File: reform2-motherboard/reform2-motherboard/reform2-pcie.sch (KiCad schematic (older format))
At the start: 31 parts, among them J10 1-2199230-6, J11 48099-5701, U11 679105700

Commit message: reform2 motherboard: add part numbers
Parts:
- C119, C121, C122, C52, C53, C54, C55, C58, C59, C60, C61: Manufacturer TDK -> Yageo; Manufacturer_No CGA3E2X8R1E104K080AE -> CC0603JPX7R9BB104
- C120: Manufacturer Taiyo Yuden -> TDK; Manufacturer_No LMK107BBJ106KALT -> CGA3E2X8R1E104K080AE
- C123, C83: Manufacturer Taiyo Yuden -> Murata; Manufacturer_No LMK107BBJ106KALT -> GRM188R60J476ME15D
- C124, C126: Manufacturer TDK -> Murata; Manufacturer_No CGA3E2X8R1E104K080AE -> GRM188R60J476ME15D
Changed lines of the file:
@@
 F 2 "Capacitor_SMD:C_0603_1608Metric" H 2000 2050 50  0001 C CNN
 F 3 "~" H 2000 2050 50  0001 C CNN
-F 4 "TDK" H 2000 2050 50  0001 C CNN "Manufacturer"
-F 5 "CGA3E2X8R1E104K080AE" H 2000 2050 50  0001 C CNN "Manufacturer_No"
+F 4 "Yageo" H 2000 2050 50  0001 C CNN "Manufacturer"
+F 5 "CC0603JPX7R9BB104" H 2000 2050 50  0001 C CNN "Manufacturer_No"
 	1    2000 2050
 	1    0    0    -1
@@
 F 2 "Capacitor_SMD:C_0603_1608Metric" H 2400 2050 50  0001 C CNN
 F 3 "~" H 2400 2050 50  0001 C CNN
-F 4 "TDK" H 2400 2050 50  0001 C CNN "Manufacturer"
-F 5 "CGA3E2X8R1E104K080AE" H 2400 2050 50  0001 C CNN "Manufacturer_No"
+F 4 "Yageo" H 2400 2050 50  0001 C CNN "Manufacturer"
+F 5 "CC0603JPX7R9BB104" H 2400 2050 50  0001 C CNN "Manufacturer_No"
 	1    2400 2050
 	1    0    0    -1
@@
 F 2 "Capacitor_SMD:C_0603_1608Metric" H 2800 2050 50  0001 C CNN
 F 3 "~" H 2800 2050 50  0001 C CNN
-F 4 "TDK" H 2800 2050 50  0001 C CNN "Manufacturer"
-F 5 "CGA3E2X8R1E104K080AE" H 2800 2050 50  0001 C CNN "Manufacturer_No"
+F 4 "Yageo" H 2800 2050 50  0001 C CNN "Manufacturer"
+F 5 "CC0603JPX7R9BB104" H 2800 2050 50  0001 C CNN "Manufacturer_No"
 	1    2800 2050
 	1    0    0    -1
@@
 F 2 "Capacitor_SMD:C_0603_1608Metric" H 3200 2050 50  0001 C CNN
 F 3 "~" H 3200 2050 50  0001 C CNN
-F 4 "TDK" H 3200 2050 50  0001 C CNN "Manufacturer"
-F 5 "CGA3E2X8R1E104K080AE" H 3200 2050 50  0001 C CNN "Manufacturer_No"
+F 4 "Yageo" H 3200 2050 50  0001 C CNN "Manufacturer"
+F 5 "CC0603JPX7R9BB104" H 3200 2050 50  0001 C CNN "Manufacturer_No"
 	1    3200 2050
 	1    0    0    -1
@@
 F 2 "Capacitor_SMD:C_0603_1608Metric" H 7400 1900 50  0001 C CNN
 F 3 "~" H 7400 1900 50  0001 C CNN
-F 4 "TDK" H 7400 1900 50  0001 C CNN "Manufacturer"
-F 5 "CGA3E2X8R1E104K080AE" H 7400 1900 50  0001 C CNN "Manufacturer_No"
+F 4 "Yageo" H 7400 1900 50  0001 C CNN "Manufacturer"
+F 5 "CC0603JPX7R9BB104" H 7400 1900 50  0001 C CNN "Manufacturer_No"
 	1    7400 1900
 	1    0    0    -1
@@
 F 2 "Capacitor_SMD:C_0603_1608Metric" H 7800 1900 50  0001 C CNN
 F 3 "~" H 7800 1900 50  0001 C CNN
-F 4 "TDK" H 7800 1900 50  0001 C CNN "Manufacturer"
-F 5 "CGA3E2X8R1E104K080AE" H 7800 1900 50  0001 C CNN "Manufacturer_No"
+F 4 "Yageo" H 7800 1900 50  0001 C CNN "Manufacturer"
+F 5 "CC0603JPX7R9BB104" H 7800 1900 50  0001 C CNN "Manufacturer_No"
 	1    7800 1900
 	1    0    0    -1
@@
 F 2 "Capacitor_SMD:C_0603_1608Metric" H 8200 1900 50  0001 C CNN
 F 3 "~" H 8200 1900 50  0001 C CNN
-F 4 "TDK" H 8200 1900 50  0001 C CNN "Manufacturer"
-F 5 "CGA3E2X8R1E104K080AE" H 8200 1900 50  0001 C CNN "Manufacturer_No"
+F 4 "Yageo" H 8200 1900 50  0001 C CNN "Manufacturer"
+F 5 "CC0603JPX7R9BB104" H 8200 1900 50  0001 C CNN "Manufacturer_No"
 	1    8200 1900
 	1    0    0    -1
@@
 F 2 "Capacitor_SMD:C_0603_1608Metric" H 8600 1900 50  0001 C CNN
 F 3 "~" H 8600 1900 50  0001 C CNN
-F 4 "TDK" H 8600 1900 50  0001 C CNN "Manufacturer"
-F 5 "CGA3E2X8R1E104K080AE" H 8600 1900 50  0001 C CNN "Manufacturer_No"
+F 4 "Yageo" H 8600 1900 50  0001 C CNN "Manufacturer"
+F 5 "CC0603JPX7R9BB104" H 8600 1900 50  0001 C CNN "Manufacturer_No"
 	1    8600 1900
 	1    0    0    -1
@@
 F 2 "Capacitor_SMD:C_0603_1608Metric" H 7050 4650 50  0001 C CNN
 F 3 "~" H 7050 4650 50  0001 C CNN
-F 4 "TDK" H 7050 4650 50  0001 C CNN "Manufacturer"
-F 5 "CGA3E2X8R1E104K080AE" H 7050 4650 50  0001 C CNN "Manufacturer_No"
+F 4 "Yageo" H 7050 4650 50  0001 C CNN "Manufacturer"
+F 5 "CC0603JPX7R9BB104" H 7050 4650 50  0001 C CNN "Manufacturer_No"
 	1    7050 4650
 	0    1    1    0
@@
 F 2 "Capacitor_SMD:C_0603_1608Metric" H 6750 4750 50  0001 C CNN
 F 3 "~" H 6750 4750 50  0001 C CNN
-F 4 "TDK" H 6750 4750 50  0001 C CNN "Manufacturer"
-F 5 "CGA3E2X8R1E104K080AE" H 6750 4750 50  0001 C CNN "Manufacturer_No"
+F 4 "Yageo" H 6750 4750 50  0001 C CNN "Manufacturer"
+F 5 "CC0603JPX7R9BB104" H 6750 4750 50  0001 C CNN "Manufacturer_No"
 	1    6750 4750
 	0    1    1    0
@@
 F 2 "Capacitor_SMD:C_0603_1608Metric" H 5200 2400 50  0001 C CNN
 F 3 "~" H 5200 2400 50  0001 C CNN
-F 4 "Taiyo Yuden" H 5200 2400 50  0001 C CNN "Manufacturer"
-F 5 "LMK107BBJ106KALT" H 5200 2400 50  0001 C CNN "Manufacturer_No"
+F 4 "TDK" H 5200 2400 50  0001 C CNN "Manufacturer"
+F 5 "CGA3E2X8R1E104K080AE" H 5200 2400 50  0001 C CNN "Manufacturer_No"
 	1    5200 2400
 	1    0    0    -1
@@
 F 2 "Capacitor_SMD:C_0603_1608Metric" H 4800 2400 50  0001 C CNN
 F 3 "~" H 4800 2400 50  0001 C CNN
-F 4 "TDK" H 4800 2400 50  0001 C CNN "Manufacturer"
-F 5 "CGA3E2X8R1E104K080AE" H 4800 2400 50  0001 C CNN "Manufacturer_No"
+F 4 "Yageo" H 4800 2400 50  0001 C CNN "Manufacturer"
+F 5 "CC0603JPX7R9BB104" H 4800 2400 50  0001 C CNN "Manufacturer_No"
 	1    4800 2400
 	1    0    0    -1
@@
 F 2 "Capacitor_SMD:C_0603_1608Metric" H 3600 2050 50  0001 C CNN
 F 3 "~" H 3600 2050 50  0001 C CNN
-F 4 "Taiyo Yuden" H 3600 2050 50  0001 C CNN "Manufacturer"
-F 5 "LMK107BBJ106KALT" H 3600 2050 50  0001 C CNN "Manufacturer_No"
+F 4 "Murata" H 3600 2050 50  0001 C CNN "Manufacturer"
+F 5 "GRM188R60J476ME15D" H 3600 2050 50  0001 C CNN "Manufacturer_No"
 	1    3600 2050
 	1    0    0    -1
@@
 F 2 "Capacitor_SMD:C_0603_1608Metric" H 4000 2050 50  0001 C CNN
 F 3 "~" H 4000 2050 50  0001 C CNN
-F 4 "Taiyo Yuden" H 4000 2050 50  0001 C CNN "Manufacturer"
-F 5 "LMK107BBJ106KALT" H 4000 2050 50  0001 C CNN "Manufacturer_No"
+F 4 "Murata" H 4000 2050 50  0001 C CNN "Manufacturer"
+F 5 "GRM188R60J476ME15D" H 4000 2050 50  0001 C CNN "Manufacturer_No"
 	1    4000 2050
 	1    0    0    -1
@@
 F 2 "Capacitor_SMD:C_0603_1608Metric" H 9000 1900 50  0001 C CNN
 F 3 "~" H 9000 1900 50  0001 C CNN
-F 4 "TDK" H 9000 1900 50  0001 C CNN "Manufacturer"
-F 5 "CGA3E2X8R1E104K080AE" H 9000 1900 50  0001 C CNN "Manufacturer_No"
+F 4 "Murata" H 9000 1900 50  0001 C CNN "Manufacturer"
+F 5 "GRM188R60J476ME15D" H 9000 1900 50  0001 C CNN "Manufacturer_No"
 	1    9000 1900
 	1    0    0    -1
@@
 F 2 "Capacitor_SMD:C_0603_1608Metric" H 9400 1900 50  0001 C CNN
 F 3 "~" H 9400 1900 50  0001 C CNN
-F 4 "TDK" H 9400 1900 50  0001 C CNN "Manufacturer"
-F 5 "CGA3E2X8R1E104K080AE" H 9400 1900 50  0001 C CNN "Manufacturer_No"
+F 4 "Murata" H 9400 1900 50  0001 C CNN "Manufacturer"
+F 5 "GRM188R60J476ME15D" H 9400 1900 50  0001 C CNN "Manufacturer_No"
 	1    9400 1900
 	1    0    0    -1

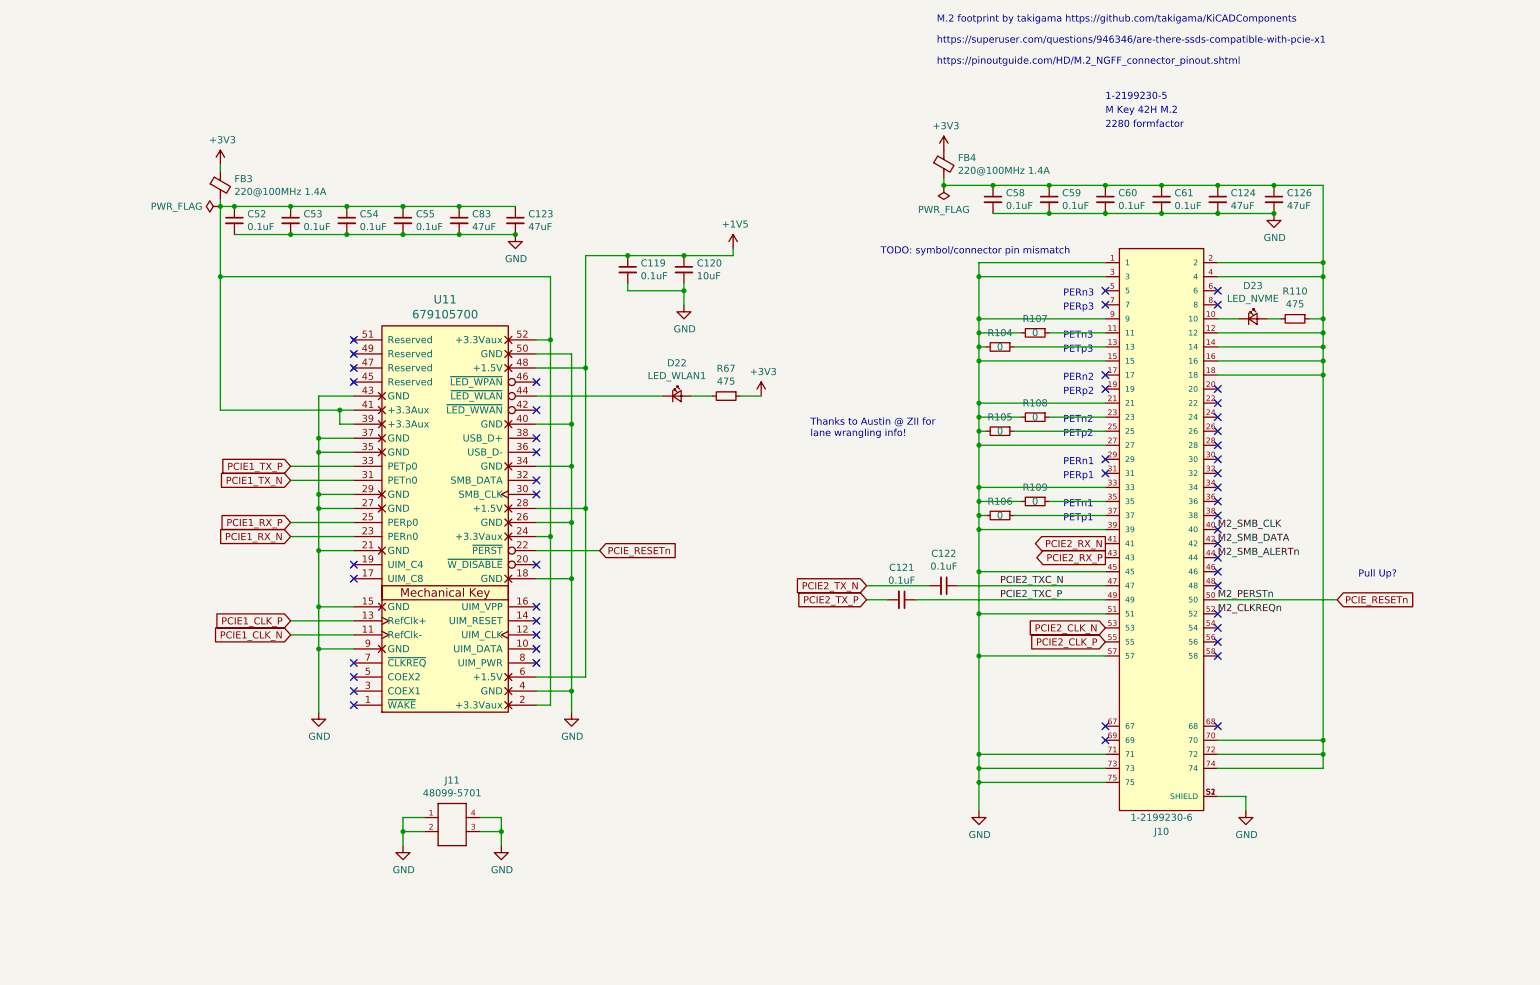
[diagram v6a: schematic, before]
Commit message: Reform 2 Rev 2 WIP: fixed various Rev 1 bugs; consolidate battery connector; consolidate 5v powers; make power rails switchable by LPC; exchange TUSB QFN for TQFP; remove eDP FPC; fixes holes; add SD level shifter; add PCIe clock generator; reduce JTAG footprint
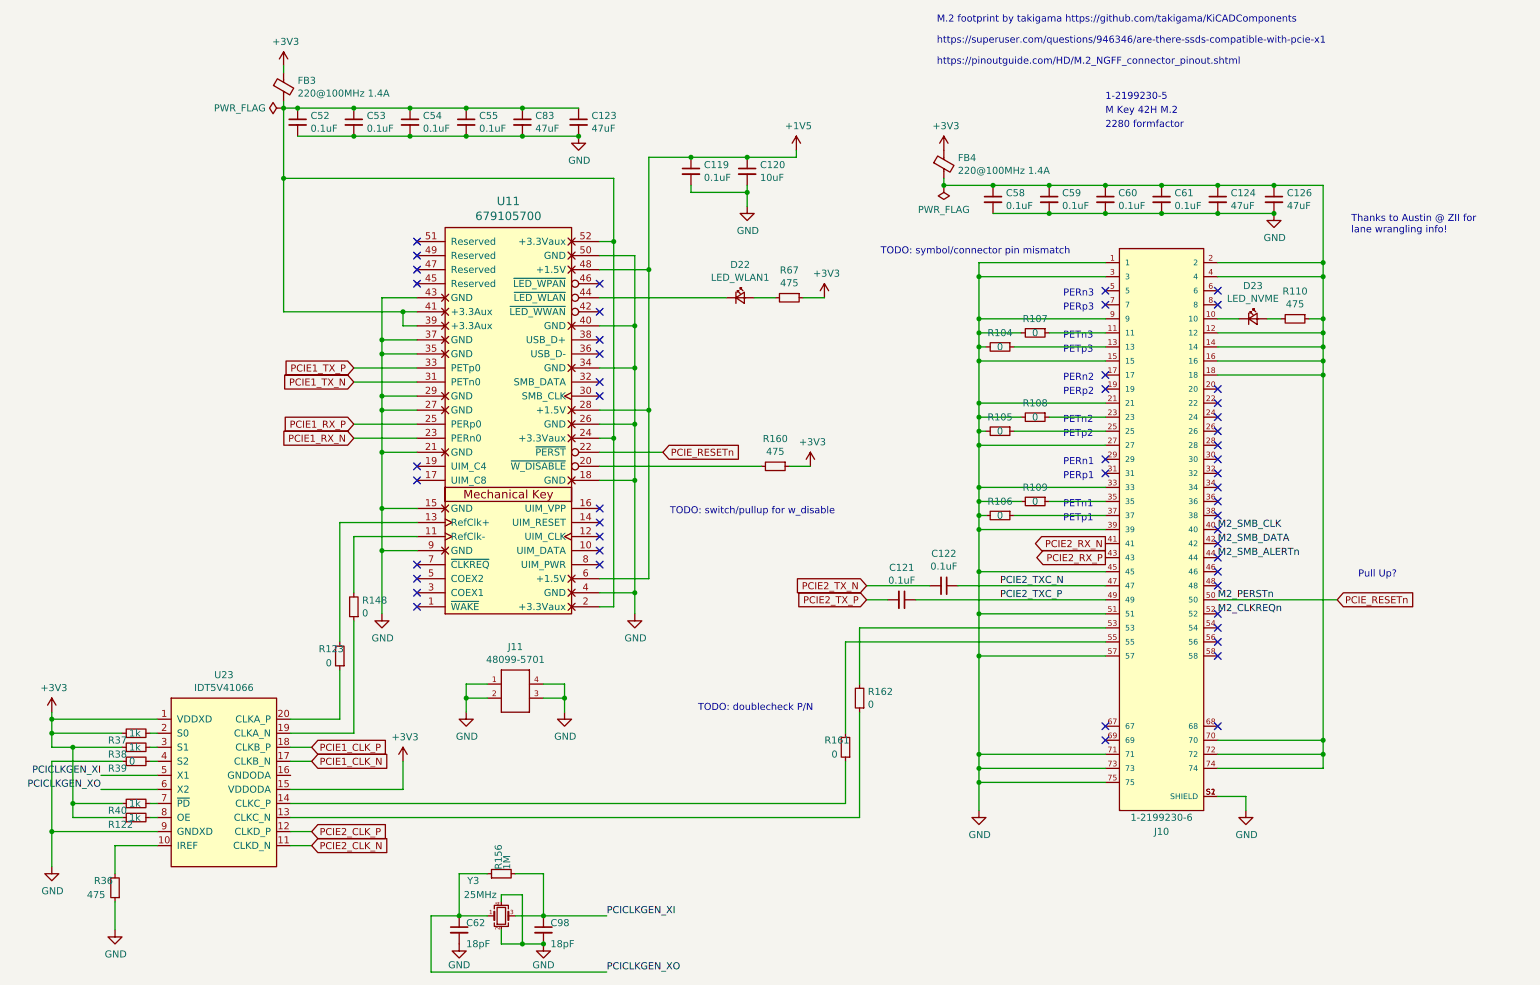
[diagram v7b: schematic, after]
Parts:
- added C62, C98: 18pF, Capacitor_SMD:C_0603_1608Metric, symbol reform2-motherboard-rescue:C_Small-reform-motherboard-rescue
- added R122, R37, R38, R40: 1k, Resistor_SMD:R_0603_1608Metric, symbol Device:R_Small
- added R123, R148, R161, R162, R39: 0, Resistor_SMD:R_0603_1608Metric, symbol Device:R_Small
- added R156: 1M, Resistor_SMD:R_0603_1608Metric, symbol reform2-motherboard-rescue:R_Small-reform-motherboard-rescue
- added R160, R36: 475, Resistor_SMD:R_0603_1608Metric, symbol Device:R_Small
- added U23: IDT5V41066, Package_SO:TSSOP-20_4.4x6.5mm_P0.65mm, symbol reform2:IDT5V41066
- added Y3: 25MHz, Crystal:Crystal_SMD_Abracon_ABM8G-4Pin_3.2x2.5mm, symbol Device:Crystal_GND24_Small
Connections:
- net +3V3: now also R122.1, R160.1, R37.1, R38.1, R40.1, U23.1 (VDDXD), U23.15 (VDDODA)
- net GND: now also C62.2, C98.2, R36.1, R39.1, U23.9 (GNDXD), Y3.2, Y3.4
- net PCIE1_CLK_N: now also U23.17 (CLKB_N); no longer U11.11 (RefClk-)
- net PCIE1_CLK_P: now also U23.18 (CLKB_P); no longer U11.13 (RefClk+)
- net PCIE2_CLK_N: now also U23.11 (CLKD_N); no longer J10.53
- net PCIE2_CLK_P: now also U23.12 (CLKD_P); no longer J10.55
- net at U11.20 (~W_DISABLE): now also R160.2
- new net: R148.2, U11.11 (RefClk-)
- new net: R123.2, U11.13 (RefClk+)
- new net: R162.1, U23.13 (CLKC_N)
- new net: J10.53, R162.2
- new net: R161.1, U23.14 (CLKC_P)
- new net: J10.55, R161.2
- new net: R148.1, U23.19 (CLKA_N)
- new net: R123.1, U23.20 (CLKA_P)
- new net: R36.2, U23.10 (IREF)
- new net: R37.2, U23.2 (S0)
- new net: R38.2, U23.3 (S1)
- new net: R40.2, U23.7 (~PD)
- new net: R39.2, U23.4 (S2)
- new net: R122.2, U23.8 (OE)
- new net PCICLKGEN_XI: C98.1, R156.2, U23.5 (X1), Y3.3
- new net PCICLKGEN_XO: C62.1, R156.1, U23.6 (X2), Y3.1
- no-connect marks 52 -> 51
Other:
- note added: "TODO: doublecheck P/N"
- note added: "TODO: switch/pullup for w_disable"
- moved on the sheet: C119, C120, C123, C52, C53, C54, C55, C83, D22, FB3, J11, R67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

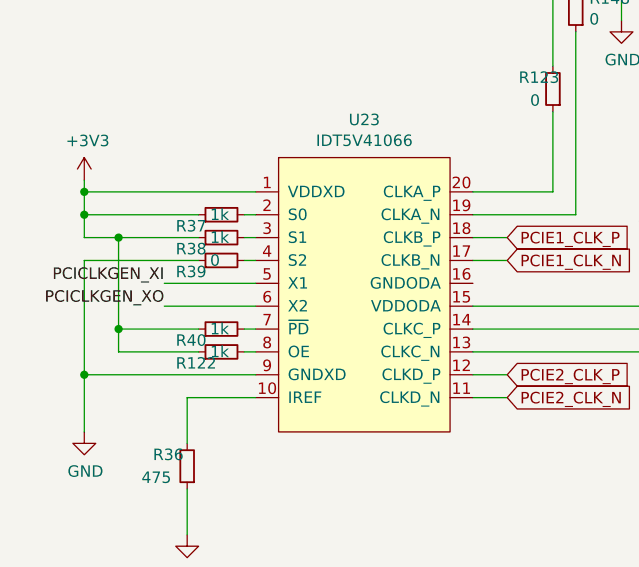
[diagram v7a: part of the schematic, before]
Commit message: reform2 motherboard: finalize BOM
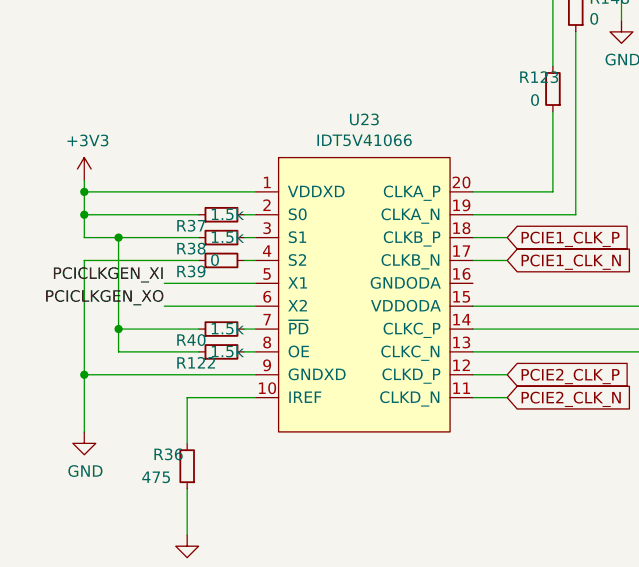
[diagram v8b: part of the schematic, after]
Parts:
- C120: Manufacturer TDK -> Murata; Manufacturer_No CGA3E2X8R1E104K080AE -> GRM188R6YA106MA73D
- R122, R37, R38, R40: value 1k -> 1.5k; Manufacturer (none) -> Yageo; Manufacturer_No (none) -> RC0603FR-071K5L
- R123, R148, R161, R162, R39: Manufacturer (none) -> Vishay Dale; Manufacturer_No (none) -> CRCW06030000Z0EAC
- R36: Manufacturer (none) -> Yageo; Manufacturer_No (none) -> RC0603FR-07475RL
- U23: Manufacturer (none) -> IDT; Manufacturer_No (none) -> 5V41066PGGI8
- Y3: Manufacturer_No (none) -> ABM8AIG-25.000MHz-R40-4-T
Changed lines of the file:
@@
 F 2 "Capacitor_SMD:C_0603_1608Metric" H 5650 1700 50  0001 C CNN
 F 3 "~" H 5650 1700 50  0001 C CNN
-F 4 "TDK" H 5650 1700 50  0001 C CNN "Manufacturer"
-F 5 "CGA3E2X8R1E104K080AE" H 5650 1700 50  0001 C CNN "Manufacturer_No"
+F 4 "Murata" H 5650 1700 50  0001 C CNN "Manufacturer"
+F 5 "GRM188R6YA106MA73D" H 5650 1700 50  0001 C CNN "Manufacturer_No"
 	1    5650 1700
 	1    0    0    -1
@@
 F 2 "Resistor_SMD:R_0603_1608Metric" H 6450 5450 50  0001 C CNN
 F 3 "~" H 6450 5450 50  0001 C CNN
+F 4 "Vishay Dale" H 6450 5450 50  0001 C CNN "Manufacturer"
+F 5 "CRCW06030000Z0EAC" H 6450 5450 50  0001 C CNN "Manufacturer_No"
 	1    6450 5450
 	-1   0    0    1
@@
 F 2 "Resistor_SMD:R_0603_1608Metric" H 6350 5800 50  0001 C CNN
 F 3 "~" H 6350 5800 50  0001 C CNN
+F 4 "Vishay Dale" H 6350 5800 50  0001 C CNN "Manufacturer"
+F 5 "CRCW06030000Z0EAC" H 6350 5800 50  0001 C CNN "Manufacturer_No"
 	1    6350 5800
 	-1   0    0    1
@@
 F 2 "Resistor_SMD:R_0603_1608Metric" H 2850 4800 50  0001 C CNN
 F 3 "~" H 2850 4800 50  0001 C CNN
+F 4 "Vishay Dale" H 2850 4800 50  0001 C CNN "Manufacturer"
+F 5 "CRCW06030000Z0EAC" H 2850 4800 50  0001 C CNN "Manufacturer_No"
 	1    2850 4800
 	-1   0    0    1
@@
 F 2 "Resistor_SMD:R_0603_1608Metric" H 2750 5150 50  0001 C CNN
 F 3 "~" H 2750 5150 50  0001 C CNN
+F 4 "Vishay Dale" H 2750 5150 50  0001 C CNN "Manufacturer"
+F 5 "CRCW06030000Z0EAC" H 2750 5150 50  0001 C CNN "Manufacturer_No"
 	1    2750 5150
 	-1   0    0    1
@@
 F 2 "Resistor_SMD:R_0603_1608Metric" H 1150 6800 50  0001 C CNN
 F 3 "~" H 1150 6800 50  0001 C CNN
+F 4 "Yageo" H 1150 6800 50  0001 C CNN "Manufacturer"
+F 5 "RC0603FR-07475RL" H 1150 6800 50  0001 C CNN "Manufacturer_No"
 	1    1150 6800
 	-1   0    0    1
@@
 F 3 "" H 3900 7000 50  0001 C CNN
 F 4 "Abracon" H 3900 7000 50  0001 C CNN "Manufacturer"
+F 5 "ABM8AIG-25.000MHz-R40-4-T" H 3900 7000 50  0001 C CNN "Manufacturer_No"
 	1    3900 7000
 	1    0    0    -1
@@
 P 1300 5700
 F 0 "R37" V 1250 5900 50  0000 R CNN
-F 1 "1k" V 1300 5750 50  0000 R CNN
+F 1 "1.5k" V 1300 5750 50  0000 R CNN
 F 2 "Resistor_SMD:R_0603_1608Metric" H 1300 5700 50  0001 C CNN
 F 3 "~" H 1300 5700 50  0001 C CNN
+F 4 "Yageo" H 1300 5700 50  0001 C CNN "Manufacturer"
+F 5 "RC0603FR-071K5L" H 1300 5700 50  0001 C CNN "Manufacturer_No"
 	1    1300 5700
 	0    -1   -1   0
@@
 P 1300 5800
 F 0 "R38" V 1250 6000 50  0000 R CNN
-F 1 "1k" V 1300 5850 50  0000 R CNN
+F 1 "1.5k" V 1300 5850 50  0000 R CNN
 F 2 "Resistor_SMD:R_0603_1608Metric" H 1300 5800 50  0001 C CNN
 F 3 "~" H 1300 5800 50  0001 C CNN
+F 4 "Yageo" H 1300 5800 50  0001 C CNN "Manufacturer"
+F 5 "RC0603FR-071K5L" H 1300 5800 50  0001 C CNN "Manufacturer_No"
 	1    1300 5800
 	0    -1   -1   0
@@
 F 2 "Resistor_SMD:R_0603_1608Metric" H 1300 5900 50  0001 C CNN
 F 3 "~" H 1300 5900 50  0001 C CNN
+F 4 "Vishay Dale" H 1300 5900 50  0001 C CNN "Manufacturer"
+F 5 "CRCW06030000Z0EAC" H 1300 5900 50  0001 C CNN "Manufacturer_No"
 	1    1300 5900
 	0    -1   -1   0
@@
 P 1300 6200
 F 0 "R40" V 1250 6400 50  0000 R CNN
-F 1 "1k" V 1300 6250 50  0000 R CNN
+F 1 "1.5k" V 1300 6250 50  0000 R CNN
 F 2 "Resistor_SMD:R_0603_1608Metric" H 1300 6200 50  0001 C CNN
 F 3 "~" H 1300 6200 50  0001 C CNN
+F 4 "Yageo" H 1300 6200 50  0001 C CNN "Manufacturer"
+F 5 "RC0603FR-071K5L" H 1300 6200 50  0001 C CNN "Manufacturer_No"
 	1    1300 6200
 	0    -1   -1   0
@@
 F 2 "Package_SO:TSSOP-20_4.4x6.5mm_P0.65mm" H 1950 6000 50  0001 C CNN
 F 3 "https://www.idt.com/document/dst/5v41066-datasheet" H 1950 6000 50  0001 C CNN
+F 4 "IDT" H 1950 6000 50  0001 C CNN "Manufacturer"
+F 5 "5V41066PGGI8" H 1950 6000 50  0001 C CNN "Manufacturer_No"
 	1    1950 6000
 	1    0    0    -1
@@
 P 1300 6300
 F 0 "R122" V 1250 6500 50  0000 R CNN
-F 1 "1k" V 1300 6350 50  0000 R CNN
+F 1 "1.5k" V 1300 6350 50  0000 R CNN
 F 2 "Resistor_SMD:R_0603_1608Metric" H 1300 6300 50  0001 C CNN
 F 3 "~" H 1300 6300 50  0001 C CNN
+F 4 "Yageo" H 1300 6300 50  0001 C CNN "Manufacturer"
+F 5 "RC0603FR-071K5L" H 1300 6300 50  0001 C CNN "Manufacturer_No"
 	1    1300 6300
 	0    -1   -1   0
